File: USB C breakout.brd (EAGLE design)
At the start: 21 x 16 mm, 6 parts, among them J1 TYPE-C-31-M-12, X1 TSW-108-07-G-S

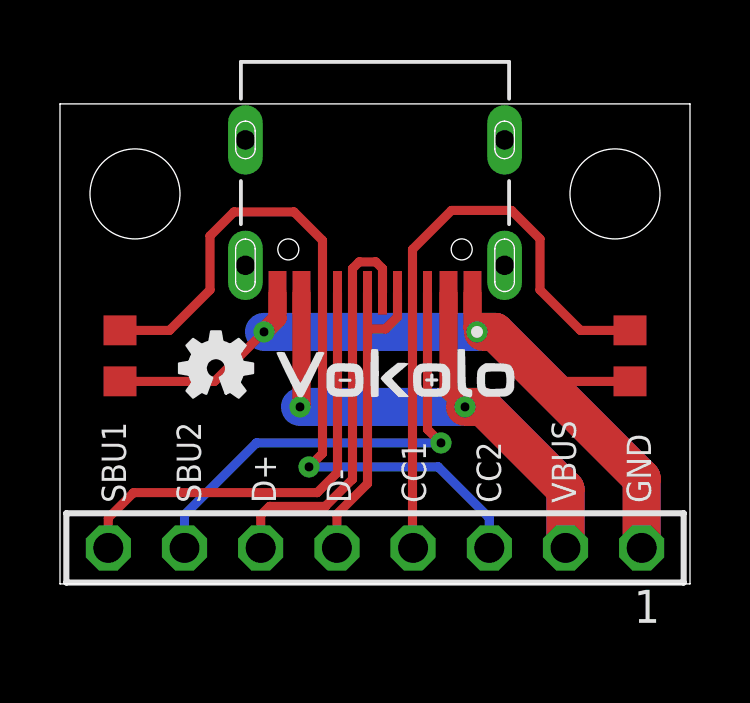
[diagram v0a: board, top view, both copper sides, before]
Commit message: Add files via upload
New version USB-C breakout board.
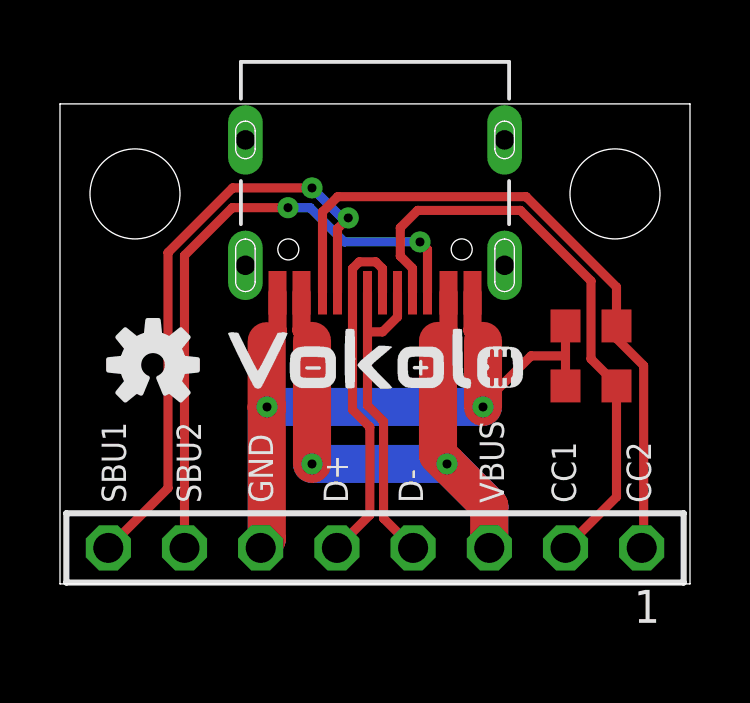
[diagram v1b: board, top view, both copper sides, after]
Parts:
- LOGO1: value OSHW-LOGOMINI -> OSHW-LOGOS; device SparkFun-Aesthetics:OSHW-LOGO-MINI -> SparkFun-Aesthetics:OSHW-LOGO-S
- U$1: value LOGO_VOKOLO9,7MM -> LOGO_VOKOLO12MM; device logo_vokolo:LOGO_VOKOLO_8MM -> logo_vokolo:LOGO_VOKOLO_9,8MM
- moved R1 15.7 mm to (17.7, 8.60), turned to 0 degrees
- moved LOGO1 2.10 mm to (3.10, 7.30)
- moved R2 1.64 mm to (17.7, 6.60), turned to 180 degrees
- moved U$1 0.67 mm to (6.60, 6.50)
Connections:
- net CC1: now also X1.2; no longer X1.4
- net CC2: now also X1.1; no longer X1.3
- net D+: now also X1.5; no longer X1.6
- net D-: now also X1.4; no longer X1.5
- net GND: now also X1.6; no longer X1.1
- net VBUS: now also X1.3; no longer X1.2
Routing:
- net GND: track 40.2 -> 30.3 mm
- net SBU1: track 15.3 -> 20.6 mm, vias 0 -> 2
- net SBU2: track 15.8 -> 20.5 mm, vias 1 -> 2
- net VBUS: track 26.2 -> 23.1 mm
- net CC2: track 25.3 -> 23.0 mm, vias 1 -> 0
- net D+: track 13.7 -> 12.0 mm
- net CC1: track 20.4 -> 19.9 mm
